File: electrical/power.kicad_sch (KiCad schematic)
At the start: 66 parts

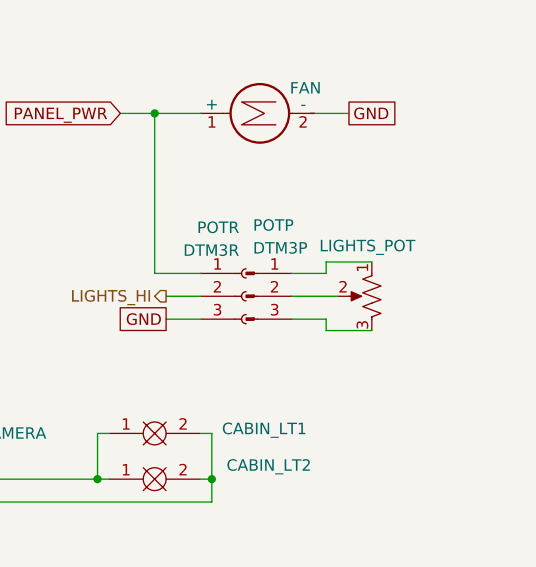
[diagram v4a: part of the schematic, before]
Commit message: Added switch to potentiometer for lights.
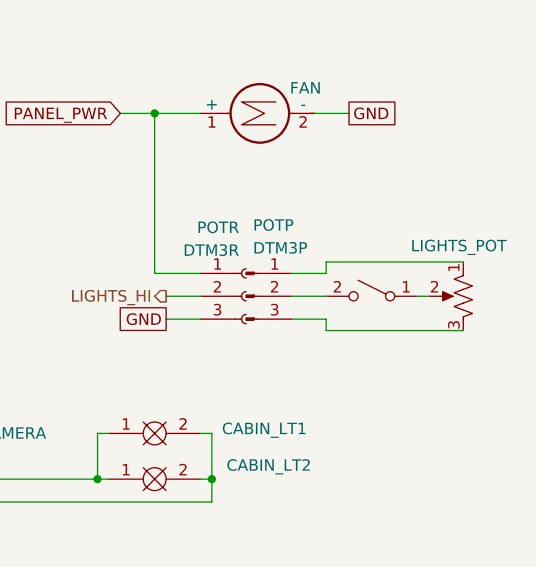
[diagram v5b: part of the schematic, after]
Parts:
- added LIGHTS_SW: ~, symbol Switch:SW_SPST
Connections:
- net at LIGHTS_POT.2: now also LIGHTS_SW.1 (A); no longer POTP.2 (Pin_2)
- new net: LIGHTS_SW.2 (B), POTP.2 (Pin_2)
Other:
- moved on the sheet: LIGHTS_POT
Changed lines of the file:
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@@
 		(title "Power Distribution")
 		(date "2025-10-19")
-		(rev "1.1.15")
+		(rev "1.1.16")
 		(company "N78HR")
 	)
@@
 	(wire
 		(pts
+			(xy 243.84 170.18) (xy 245.11 170.18)
+		)
+		(stroke
+			(width 0)
+			(type default)
+		)
+	)
+	(wire
+		(pts
 			(xy 57.15 224.79) (xy 63.5 224.79)
 		)
@@
 	(wire
 		(pts
-			(xy 233.68 166.37) (xy 238.76 166.37)
+			(xy 233.68 166.37) (xy 248.92 166.37)
 		)
 		(stroke
@@
 	(wire
 		(pts
+			(xy 229.87 170.18) (xy 233.68 170.18)
+		)
+		(stroke
+			(width 0)
+			(type default)
+		)
+	)
+	(wire
+		(pts
 			(xy 69.85 283.21) (xy 69.85 280.67)
 		)
@@
 	(wire
 		(pts
-			(xy 233.68 173.99) (xy 238.76 173.99)
+			(xy 233.68 173.99) (xy 248.92 173.99)
 		)
 		(stroke
@@
 	(wire
 		(pts
-			(xy 229.87 170.18) (xy 234.95 170.18)
-		)
-		(stroke
-			(width 0)
-			(type default)
-		)
-	)
-	(wire
-		(pts
 			(xy 57.15 100.33) (xy 62.23 100.33)
 		)
@@
 	)
 	(symbol
+		(lib_id "Switch:SW_SPST")
+		(at 238.76 170.18 0)
+		(mirror y)
+		(unit 1)
+		(exclude_from_sim no)
+		(in_bom yes)
+		(on_board yes)
+		(dnp no)
+		(property "Reference" "LIGHTS_SW"
+			(at 238.76 166.37 0)
+			(effects
+				(font
+					(size 1.27 1.27)
+				)
+				(hide yes)
+			)
+		)
+		(property "Value" "~"
+			(at 238.76 166.37 0)
+			(effects
+				(font
+					(size 1.27 1.27)
+				)
+				(hide yes)
+			)
+		)
+		(property "Footprint" ""
+			(at 238.76 170.18 0)
+			(effects
+				(font
+					(size 1.27 1.27)
+				)
+				(hide yes)
+			)
+		)
+		(property "Datasheet" "~"
+			(at 238.76 170.18 0)
+			(effects
+				(font
+					(size 1.27 1.27)
+				)
+				(hide yes)
+			)
+		)
+		(property "Description" ""
+			(at 238.76 170.18 0)
+			(effects
+				(font
+					(size 1.27 1.27)
+				)
+			)
+		)
+		(pin "2"
+		)
+		(pin "1"
+		)
+		(instances
+			(project "electrical"
+				(path "/e8ec215a-dbe2-4eba-a577-e50a0a128049/2852c073-fbc9-4469-a6bf-ba3e911c7f5a"
+					(reference "LIGHTS_SW")
+					(unit 1)
+				)
+			)
+		)
+	)
+	(symbol
 		(lib_id "Connector:Conn_01x03_Socket")
 		(at 217.17 250.19 0)
@@
 	(symbol
 		(lib_id "Device:R_Potentiometer_US")
-		(at 238.76 170.18 0)
+		(at 248.92 170.18 0)
 		(mirror y)
 		(unit 1)
@@
 		(dnp no)
 		(property "Reference" "LIGHTS_POT"
-			(at 238.252 164.592 0)
+			(at 248.412 164.592 0)
 			(effects
 				(font
@@
 		)
 		(property "Value" "R_Potentiometer_US"
-			(at 245.11 170.18 90)
+			(at 255.27 170.18 90)
 			(effects
 				(font
@@
 		)
 		(property "Footprint" ""
-			(at 238.76 170.18 0)
+			(at 248.92 170.18 0)
 			(effects
 				(font
@@
 		)
 		(property "Datasheet" "~"
-			(at 238.76 170.18 0)
+			(at 248.92 170.18 0)
 			(effects
 				(font
@@
 		)
 		(property "Description" "Potentiometer, US symbol"
-			(at 238.76 170.18 0)
+			(at 248.92 170.18 0)
 			(effects
 				(font

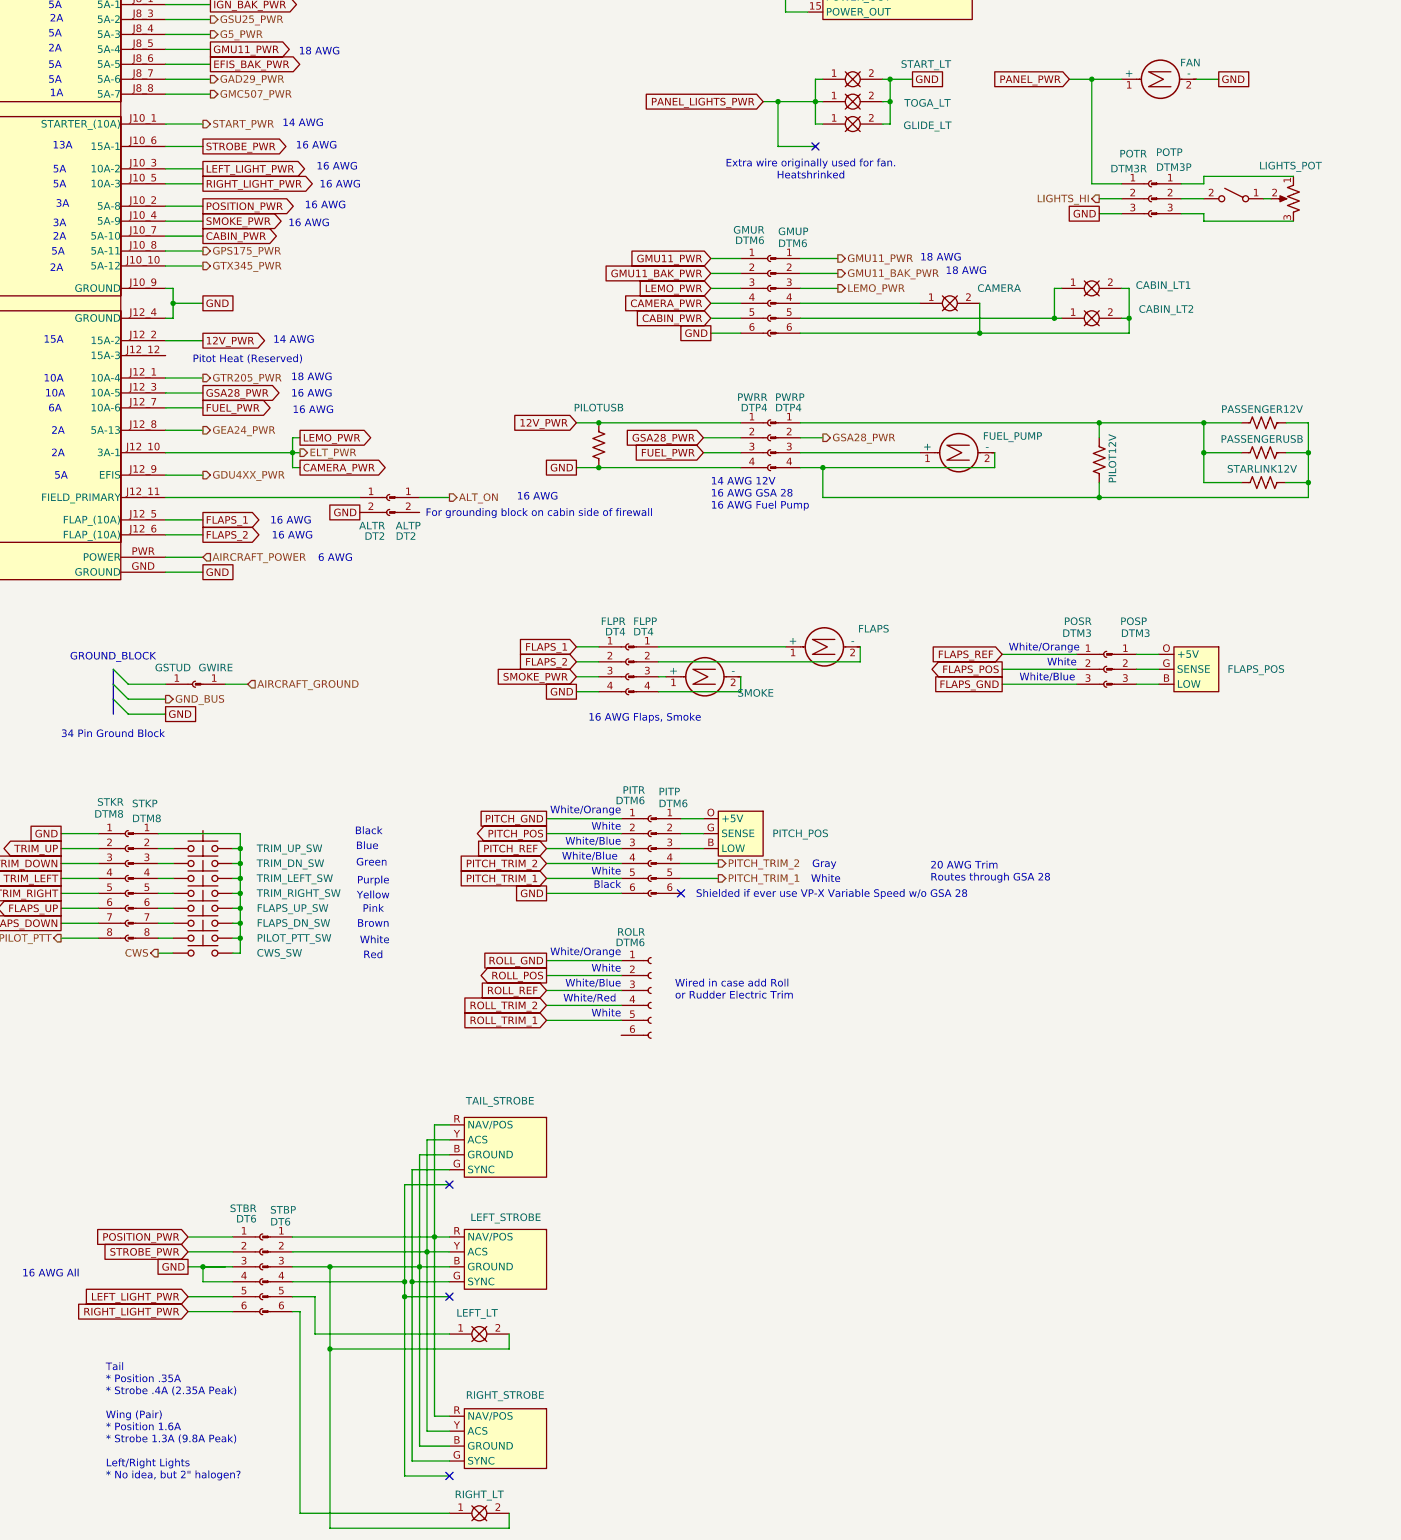
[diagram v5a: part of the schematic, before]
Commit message: Removed switch from POT. Moved strobes to be separate, bottom/top.
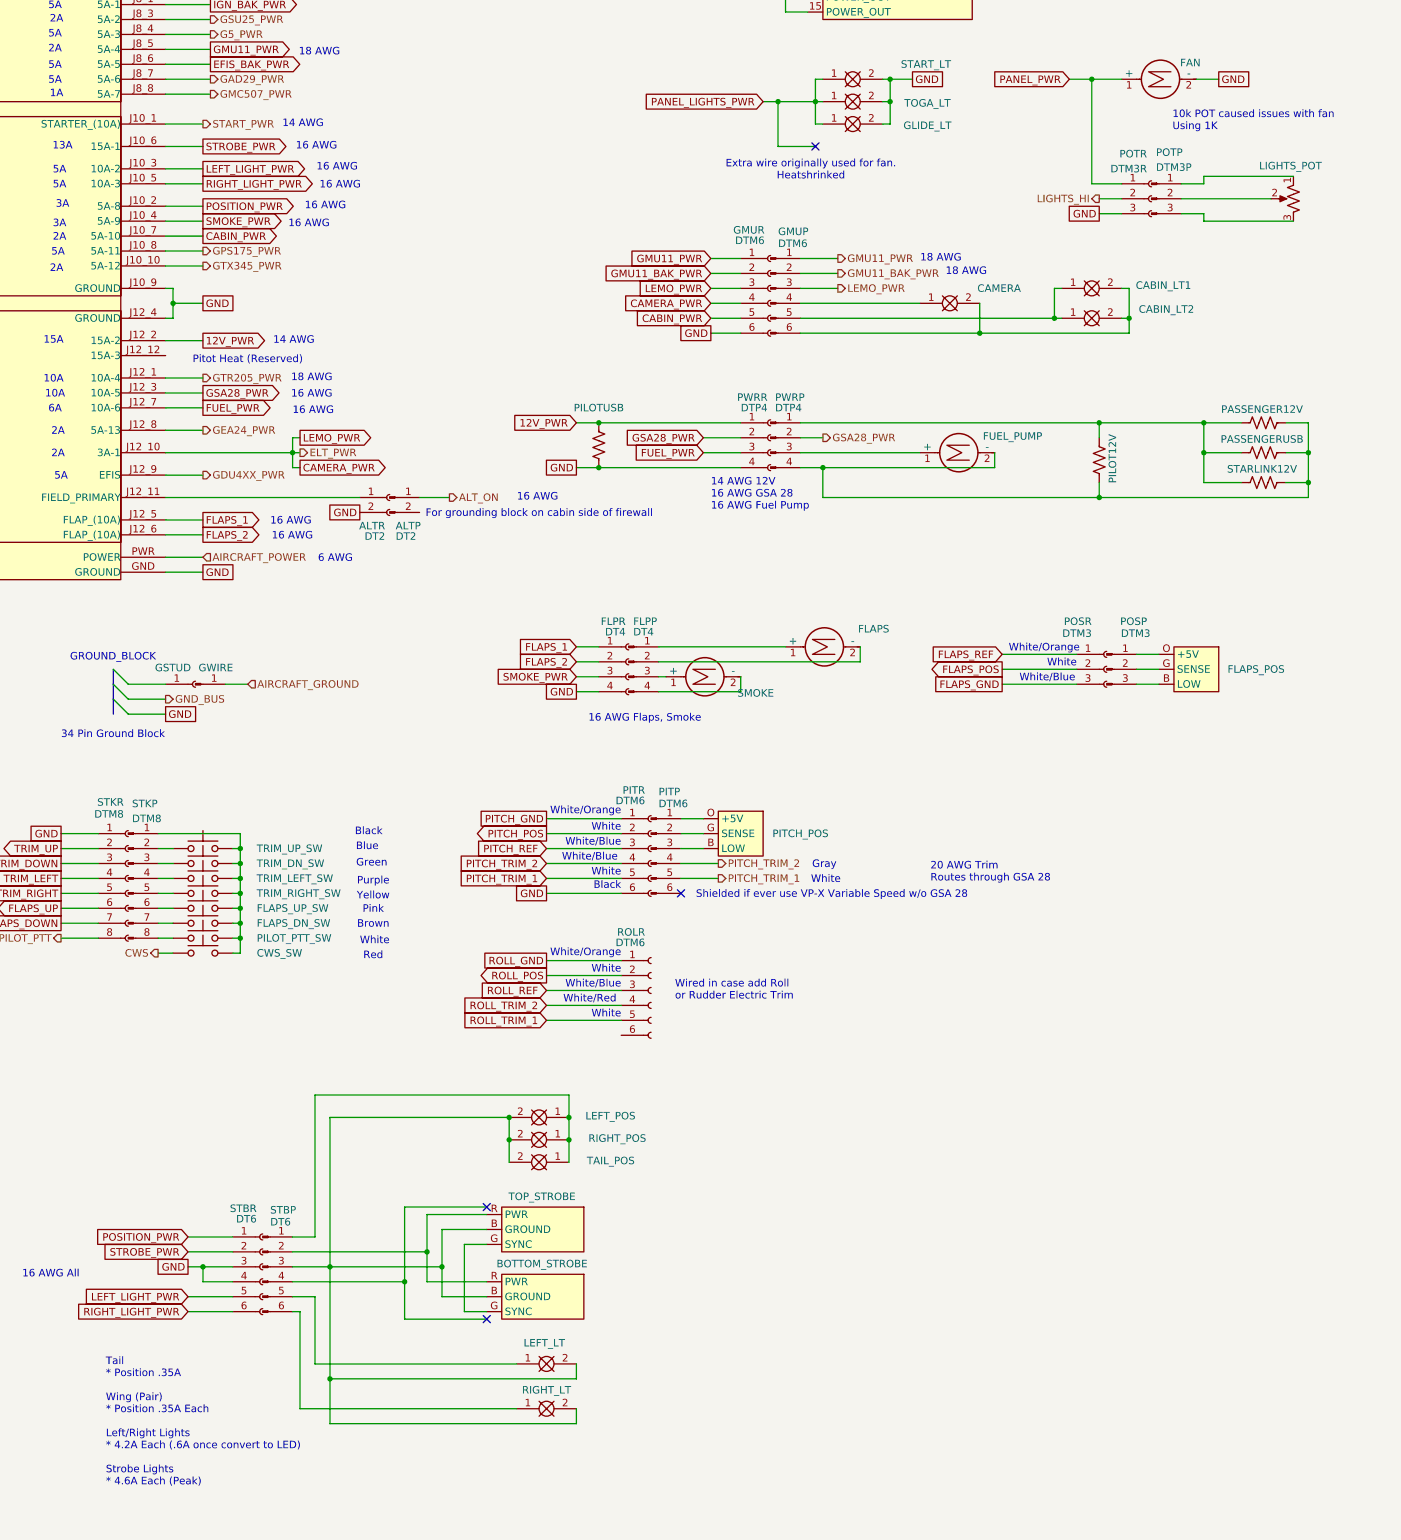
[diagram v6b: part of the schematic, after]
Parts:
- removed LEFT_STROBE, RIGHT_STROBE: ~, symbol flyerx:AeroLED_Pulsar650
- removed LIGHTS_SW: ~, symbol Switch:SW_SPST
- removed TAIL_STROBE: ~, symbol flyerx:AeroLED_SunTail550
- added BOTTOM_STROBE, TOP_STROBE: ~, symbol flyerx:Aveo_SuperNova_FS_DayLite
- added LEFT_POS, RIGHT_POS, TAIL_POS: ~, symbol flyerx:Bulb
- LIGHTS_POT: value R_Potentiometer_US -> 1K
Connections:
- net at LEFT_LT.2, RIGHT_LT.2, STBP.3 (Pin_3): now also BOTTOM_STROBE.B (GROUND), LEFT_POS.2, RIGHT_POS.2, TAIL_POS.2, TOP_STROBE.B (GROUND)
- net at STBP.1 (Pin_1): now also LEFT_POS.1, RIGHT_POS.1, TAIL_POS.1
- net at STBP.2 (Pin_2): now also BOTTOM_STROBE.R (PWR), TOP_STROBE.R (PWR)
- net at LIGHTS_POT.2: now also POTP.2 (Pin_2)
- new net: BOTTOM_STROBE.G (SYNC), TOP_STROBE.G (SYNC)
- no-connect marks 8 -> 7
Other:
- note added: "10k POT caused issues with fan Using 1K"
- note added: "Tail * Position .35A Wing (Pair) * Position .35A Each Left/Right Lights * 4.2A Each (.6A once convert to LED) Strobe Lights * 4.6A Each (Peak)"
- note removed: "Tail * Position .35A * Strobe .4A (2.35A Peak) Wing (Pair) * Position 1.6A * Strobe 1.3A (9.8A Peak) Left/Right Lights * No idea, but 2" halogen?"
- moved on the sheet: LEFT_LT, RIGHT_LT

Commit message: Removed power config. Added USB-B plug for GTX 345 to GSB 15.
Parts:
- removed PILOTUSB: R_US, symbol Device:R_US
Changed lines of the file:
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@@
 	(title_block
 		(title "Power Distribution")
-		(date "2025-10-21")
-		(rev "1.1.17")
+		(date "2025-11-01")
+		(rev "1.2.1")
 		(company "N78HR")
 	)
@@
 	)
 	(junction
+		(at 129.54 208.28)
+		(diameter 0)
+		(color 0 0 0 0)
+	)
+	(junction
 		(at 220.98 190.5)
 		(diameter 0)
@@
 	)
 	(junction
-		(at 130.81 215.9)
-		(diameter 0)
-		(color 0 0 0 0)
-	)
-	(junction
 		(at 115.57 326.39)
 		(diameter 0)
@@
 	)
 	(junction
-		(at 130.81 208.28)
-		(diameter 0)
-		(color 0 0 0 0)
-	)
-	(junction
 		(at 162.56 22.86)
 		(diameter 0)
@@
 	)
 	(junction
+		(at 129.54 215.9)
+		(diameter 0)
+		(color 0 0 0 0)
+	)
+	(junction
 		(at 69.85 288.29)
 		(diameter 0)
@@
 	(wire
 		(pts
+			(xy 129.54 218.44) (xy 129.54 215.9)
+		)
+		(stroke
+			(width 0)
+			(type default)
+		)
+	)
+	(wire
+		(pts
 			(xy 179.07 153.67) (xy 180.34 153.67)
 		)
@@
 	(wire
 		(pts
-			(xy 127 208.28) (xy 130.81 208.28)
+			(xy 127 208.28) (xy 129.54 208.28)
 		)
 		(stroke
@@
 	(wire
 		(pts
+			(xy 129.54 208.28) (xy 154.94 208.28)
+		)
+		(stroke
+			(width 0)
+			(type default)
+		)
+	)
+	(wire
+		(pts
 			(xy 161.29 153.67) (xy 167.64 153.67)
 		)
@@
 	(wire
 		(pts
-			(xy 130.81 208.28) (xy 154.94 208.28)
-		)
-		(stroke
-			(width 0)
-			(type default)
-		)
-	)
-	(wire
-		(pts
 			(xy 85.09 378.46) (xy 127 378.46)
 		)
@@
 	(wire
 		(pts
-			(xy 127 215.9) (xy 130.81 215.9)
+			(xy 127 215.9) (xy 129.54 215.9)
 		)
 		(stroke
@@
 	(wire
 		(pts
-			(xy 130.81 215.9) (xy 154.94 215.9)
-		)
-		(stroke
-			(width 0)
-			(type default)
-		)
-	)
-	(wire
-		(pts
 			(xy 55.88 295.91) (xy 58.42 295.91)
 		)
@@
 	(wire
 		(pts
+			(xy 130.81 205.74) (xy 129.54 205.74)
+		)
+		(stroke
+			(width 0)
+			(type default)
+		)
+	)
+	(wire
+		(pts
 			(xy 57.15 97.79) (xy 62.23 97.79)
 		)
@@
 	(wire
 		(pts
+			(xy 129.54 205.74) (xy 129.54 208.28)
+		)
+		(stroke
+			(width 0)
+			(type default)
+		)
+	)
+	(wire
+		(pts
 			(xy 57.15 63.5) (xy 62.23 63.5)
 		)
@@
 	(wire
 		(pts
+			(xy 129.54 215.9) (xy 154.94 215.9)
+		)
+		(stroke
+			(width 0)
+			(type default)
+		)
+	)
+	(wire
+		(pts
 			(xy 165.1 185.42) (xy 171.45 185.42)
 		)
@@
 	(wire
 		(pts
+			(xy 130.81 218.44) (xy 129.54 218.44)
+		)
+		(stroke
+			(width 0)
+			(type default)
+		)
+	)
+	(wire
+		(pts
 			(xy 161.29 153.67) (xy 161.29 161.29)
 		)
@@
 		)
 	)
+	(hierarchical_label "PILOT_USB_PWR"
+		(shape output)
+		(at 130.81 205.74 0)
+		(effects
+			(font
+				(size 1.27 1.27)
+			)
+			(justify left)
+		)
+	)
+	(hierarchical_label "PILOT_USB_GND"
+		(shape passive)
+		(at 130.81 218.44 0)
+		(effects
+			(font
+				(size 1.27 1.27)
+			)
+			(justify left)
+		)
+	)
 	(hierarchical_label "GTX345_PWR"
 		(shape output)
@@
 					(unit 1)
 				)
-			)
-		)
-	)
-	(symbol
-		(lib_id "Device:R_US")
-		(at 130.81 212.09 180)
-		(unit 1)
-		(exclude_from_sim no)
-		(in_bom yes)
-		(on_board yes)
-		(dnp no)
-		(property "Reference" "PILOTUSB"
-			(at 130.81 205.74 0)
-			(effects
-				(font
-					(size 1.27 1.27)
-				)
-			)
-		)
-		(property "Value" "R_US"
-			(at 134.62 212.09 90)
-			(effects
-				(font
-					(size 1.27 1.27)
-				)
-				(hide yes)
-			)
-		)
-		(property "Footprint" ""
-			(at 129.794 211.836 90)
-			(effects
-				(font
-					(size 1.27 1.27)
-				)
-				(hide yes)
-			)
-		)
-		(property "Datasheet" "~"
-			(at 130.81 212.09 0)
-			(effects
-				(font
-					(size 1.27 1.27)
-				)
-				(hide yes)
-			)
-		)
-		(property "Description" "Resistor, US symbol"
-			(at 130.81 212.09 0)
-			(effects
-				(font
-					(size 1.27 1.27)
-				)
-				(hide yes)
-			)
-		)
-		(pin "1"
-		)
-		(pin "2"
-		)
-		(instances
-			(project ""
-				(path "/e8ec215a-dbe2-4eba-a577-e50a0a128049/2852c073-fbc9-4469-a6bf-ba3e911c7f5a"
-					(reference "PILOTUSB")
-					(unit 1)
-				)
